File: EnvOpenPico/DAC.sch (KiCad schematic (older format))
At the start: 21 parts, among them U3 PCM5100, U4 PAM8901

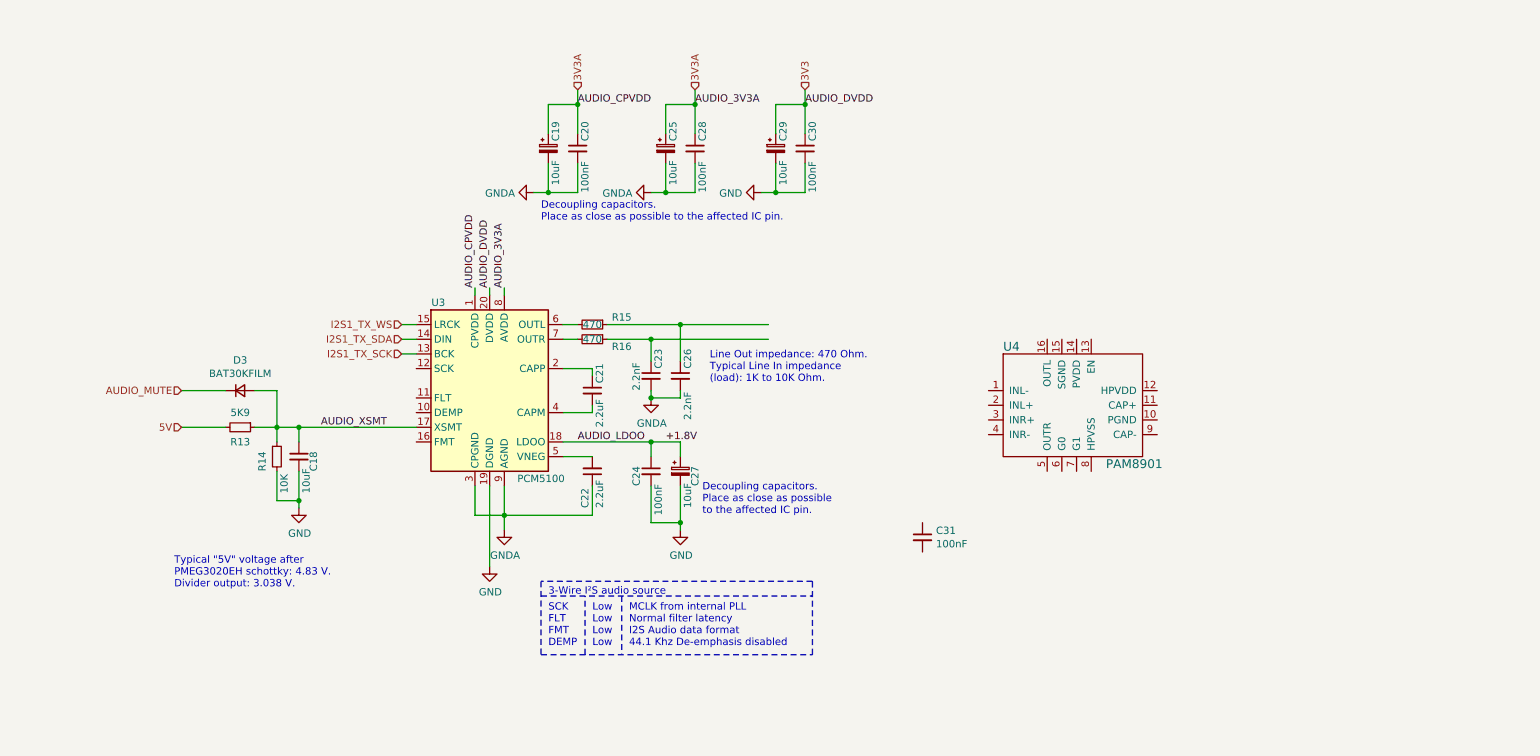
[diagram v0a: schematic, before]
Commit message: Adding audio out, adding pdf schematics
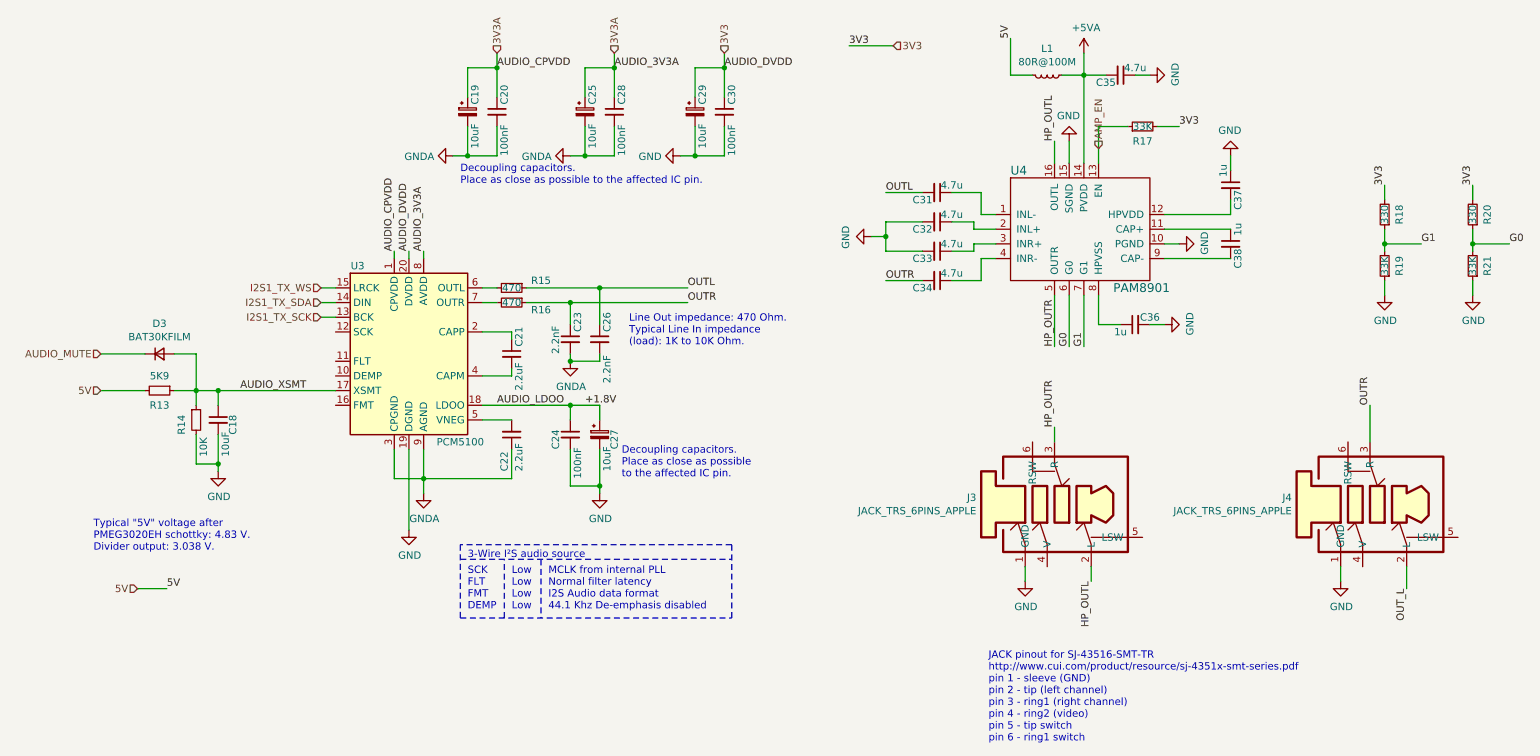
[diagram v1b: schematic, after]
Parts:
- added C32, C33, C34, C35: 4.7u, symbol Device:C_Small
- added C36, C37, C38: 1u, symbol Device:C_Small
- added J3, J4: JACK_TRS_6PINS_APPLE, symbol jack_trs_6pins_apple:JACK_TRS_6PINS_APPLE
- added L1: 80R@100M, symbol Device:L_Small
- added R17, R19, R21: 33K, symbol Device:R_Small
- added R18, R20: 330, symbol Device:R_Small
- C31: value 100nF -> 4.7u
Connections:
- net 3V3: now also R17.2, R18.2, R20.2
- net 5V: now also L1.2
- net GND: now also U4.10 (PGND), U4.15 (SGND), C32.2, C33.2, C35.1, C36.2, C37.1, J3.1 (GND), J4.1 (GND), R19.1, R21.1
- net at U4.1 (INL-): now also C31.1
- net at U4.11 (CAP+): now also C38.1
- net at U4.12 (HPVDD): now also C37.2
- net AMP_EN: now reaches U4.13 (EN)
- net AMP_EN: now also R17.1
- net +5VA: now reaches U4.14 (PVDD)
- net +5VA: now also C35.2, L1.1
- net HP_OUTL: now reaches U4.16 (OUTL)
- net HP_OUTL: now also J3.2 (L)
- net at U4.2 (INL+): now also C32.1
- net at U4.3 (INR+): now also C33.1
- net at U4.4 (INR-): now also C34.1
- net HP_OUTR: now reaches U4.5 (OUTR)
- net HP_OUTR: now also J3.3 (R)
- net G0: now reaches U4.6 (G0)
- net G0: now also R20.1, R21.2
- net G1: now reaches U4.7 (G1)
- net G1: now also R18.1, R19.2
- net at U4.8 (HPVSS): now also C36.1
- net at U4.9 (CAP-): now also C38.2
- net OUTL: now reaches C26.1, R15.1
- net OUTL: now also C31.2
- net OUTR: now reaches C23.1, R16.1
- net OUTR: now also C34.2, J4.3 (R)
- new net OUT_L: J4.2 (L)
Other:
- note added: "JACK pinout for SJ-43516-SMT-TR\nhttp://www.cui.com/product/resource/sj-4351x-smt-series.pdf\npin 1 - sleeve (GND)\npin 2 - tip (left channel)\npin 3 - ring1 (right channel)\npin 4 - ring2 (video)\npin 5 - tip switch\npin 6 - ring1 switch"
- moved on the sheet: C18, C19, C20, C21, C22, C23, C24, C25, C26, C27, C28, C29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

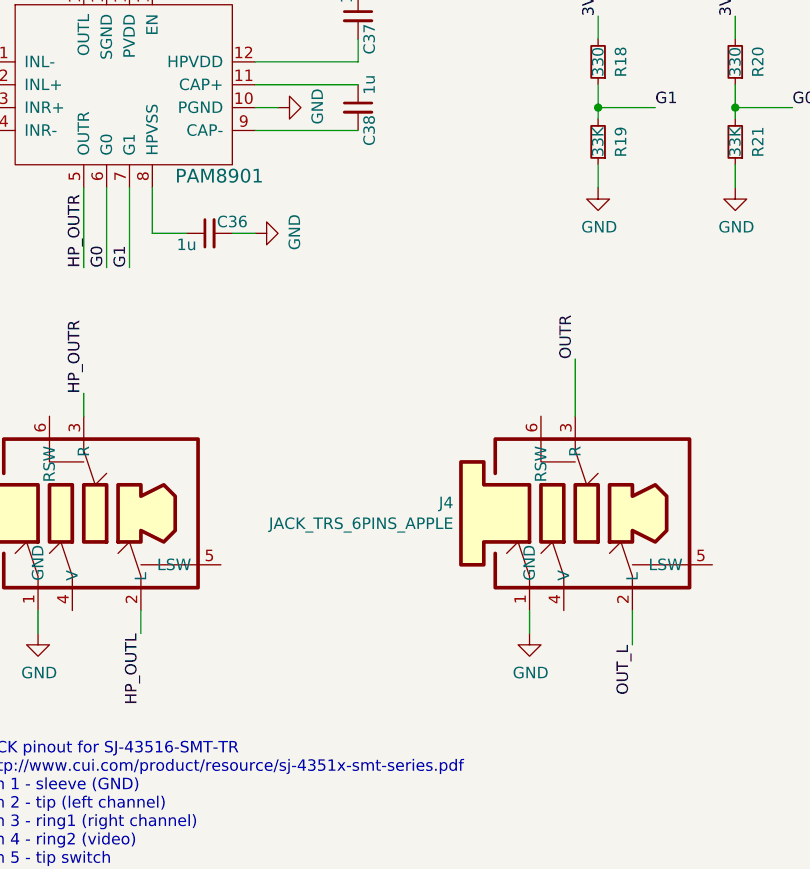
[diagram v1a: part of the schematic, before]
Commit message: Adding parts to pcb
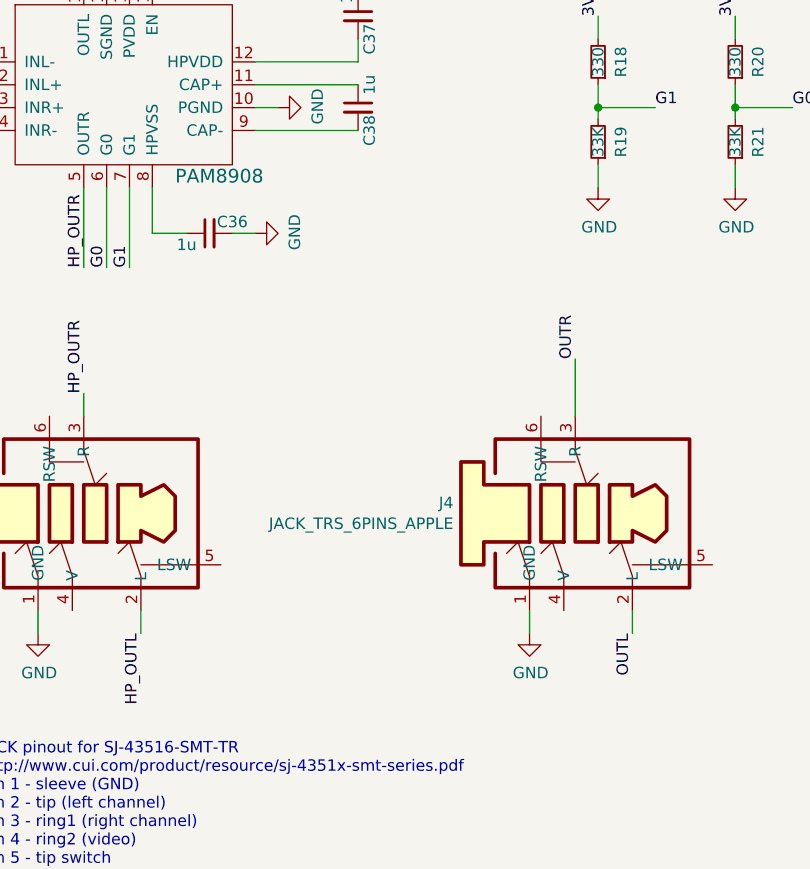
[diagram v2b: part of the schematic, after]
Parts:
- C18, C19, C25, C27, C29: footprint (none) -> Capacitor_SMD:C_1206_3216Metric
- C20, C24, C28, C30, C31, C32, C33, C34, C35, C36, C37, C38: footprint (none) -> Capacitor_SMD:C_0603_1608Metric
- C21, C22, C23, C26, R13, R14, R15, R16, R17, R18, R19, R20, R21: footprint (none) -> Capacitor_SMD:C_0402_1005Metric
- D3: footprint (none) -> Diode_SMD:D_SOD-523
- J3, J4: footprint (none) -> audio-jack:CUI_SJ-43516-SMT
- L1: footprint (none) -> Inductor_SMD:L_0603_1608Metric
- U4: value PAM8901 -> PAM8908; footprint (none) -> Package_DFN_QFN:QFN-16-1EP_3x3mm_P0.5mm_EP1.7x1.7mm_ThermalVias
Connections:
- net OUT_L is gone; now on net OUTL: J4.2 (L)
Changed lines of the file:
@@
 P 7450 1850
 F 0 "U4" H 7250 2050 60  0000 L CNN
-F 1 "PAM8901" H 7950 1250 60  0000 L CNN
-F 2 "" H 7450 2000 60  0001 C CNN
+F 1 "PAM8908" H 7950 1250 60  0000 L CNN
+F 2 "Package_DFN_QFN:QFN-16-1EP_3x3mm_P0.5mm_EP1.7x1.7mm_ThermalVias" H 7450 2000 60  0001 C CNN
 F 3 "" H 7450 2000 60  0001 C CNN
 	1    7450 1850
@@
 F 0 "C21" V 3900 2950 50  0000 L CNN
 F 1 "2.2uF" V 3900 2650 50  0000 L CNN
-F 2 "" H 3850 2900 50  0001 C CNN
-F 3 "~" H 3850 2900 50  0001 C CNN
+F 2 "Capacitor_SMD:C_0402_1005Metric" H 3850 2900 50  0001 C CNN
+F 3 "CL10A225KO8NNNC " H 3850 2900 50  0001 C CNN
 	1    3850 2900
 	1    0    0    -1
@@
 F 0 "C22" V 3900 3700 50  0000 R CNN
 F 1 "2.2uF" V 3800 3700 50  0000 R CNN
-F 2 "" H 3850 3450 50  0001 C CNN
-F 3 "~" H 3850 3450 50  0001 C CNN
+F 2 "Capacitor_SMD:C_0402_1005Metric" H 3850 3450 50  0001 C CNN
+F 3 "CL10A225KO8NNNC " H 3850 3450 50  0001 C CNN
 	1    3850 3450
 	-1   0    0    1
@@
 F 0 "R15" V 3800 2650 50  0000 C CNN
 F 1 "470" V 3850 2450 50  0000 C CNN
-F 2 "" H 3850 2450 50  0001 C CNN
+F 2 "Capacitor_SMD:C_0402_1005Metric" H 3850 2450 50  0001 C CNN
 F 3 "~" H 3850 2450 50  0001 C CNN
 	1    3850 2450
@@
 F 0 "R16" V 3900 2750 50  0000 C CNN
 F 1 "470" V 3850 2550 50  0000 C CNN
-F 2 "" H 3850 2550 50  0001 C CNN
+F 2 "Capacitor_SMD:C_0402_1005Metric" H 3850 2550 50  0001 C CNN
 F 3 "~" H 3850 2550 50  0001 C CNN
 	1    3850 2550
@@
 F 0 "C26" V 4500 2850 50  0000 L CNN
 F 1 "2.2nF" V 4500 2500 50  0000 L CNN
-F 2 "" H 4450 2800 50  0001 C CNN
+F 2 "Capacitor_SMD:C_0402_1005Metric" H 4450 2800 50  0001 C CNN
 F 3 "885012206061" H 4450 2800 50  0001 C CNN
 	1    4450 2800
@@
 F 0 "C23" V 4300 2850 50  0000 L CNN
 F 1 "2.2nF" V 4150 2700 50  0000 L CNN
-F 2 "" H 4250 2800 50  0001 C CNN
+F 2 "Capacitor_SMD:C_0402_1005Metric" H 4250 2800 50  0001 C CNN
 F 3 "885012206061" H 4250 2800 50  0001 C CNN
 	1    4250 2800
@@
 F 0 "C20" V 3800 1300 50  0000 L CNN
 F 1 "100nF" V 3800 950 50  0000 L CNN
-F 2 "" H 3750 1250 50  0001 C CNN
+F 2 "Capacitor_SMD:C_0603_1608Metric" H 3750 1250 50  0001 C CNN
 F 3 "885012206071" H 3750 1250 50  0001 C CNN
 	1    3750 1250
@@
 F 0 "C19" V 3600 1300 50  0000 L CNN
 F 1 "10uF" V 3600 1000 50  0000 L CNN
-F 2 "" H 3550 1250 50  0001 C CNN
+F 2 "Capacitor_SMD:C_1206_3216Metric" H 3550 1250 50  0001 C CNN
 F 3 "TAJA106K016RNJ" H 3550 1250 50  0001 C CNN
 	1    3550 1250
@@
 F 0 "C25" V 4400 1300 50  0000 L CNN
 F 1 "10uF" V 4400 1000 50  0000 L CNN
-F 2 "" H 4350 1250 50  0001 C CNN
+F 2 "Capacitor_SMD:C_1206_3216Metric" H 4350 1250 50  0001 C CNN
 F 3 "TAJA106K016RNJ" H 4350 1250 50  0001 C CNN
 	1    4350 1250
@@
 F 0 "C28" V 4600 1300 50  0000 L CNN
 F 1 "100nF" V 4600 950 50  0000 L CNN
-F 2 "" H 4550 1250 50  0001 C CNN
+F 2 "Capacitor_SMD:C_0603_1608Metric" H 4550 1250 50  0001 C CNN
 F 3 "885012206071" H 4550 1250 50  0001 C CNN
 	1    4550 1250
@@
 F 0 "C29" V 5150 1300 50  0000 L CNN
 F 1 "10uF" V 5150 1000 50  0000 L CNN
-F 2 "" H 5100 1250 50  0001 C CNN
+F 2 "Capacitor_SMD:C_1206_3216Metric" H 5100 1250 50  0001 C CNN
 F 3 "TAJA106K016RNJ" H 5100 1250 50  0001 C CNN
 	1    5100 1250
@@
 F 0 "C30" V 5350 1300 50  0000 L CNN
 F 1 "100nF" V 5350 950 50  0000 L CNN
-F 2 "" H 5300 1250 50  0001 C CNN
+F 2 "Capacitor_SMD:C_0603_1608Metric" H 5300 1250 50  0001 C CNN
 F 3 "885012206071" H 5300 1250 50  0001 C CNN
 	1    5300 1250
@@
 F 0 "C24" V 4150 3350 50  0000 L CNN
 F 1 "100nF" V 4300 3150 50  0000 L CNN
-F 2 "" H 4250 3450 50  0001 C CNN
+F 2 "Capacitor_SMD:C_0603_1608Metric" H 4250 3450 50  0001 C CNN
 F 3 "885012206071" H 4250 3450 50  0001 C CNN
 	1    4250 3450
@@
 F 0 "C27" V 4550 3350 50  0000 L CNN
 F 1 "10uF" V 4500 3200 50  0000 L CNN
-F 2 "" H 4450 3450 50  0001 C CNN
+F 2 "Capacitor_SMD:C_1206_3216Metric" H 4450 3450 50  0001 C CNN
 F 3 "TAJA106K016RNJ" H 4450 3450 50  0001 C CNN
 	1    4450 3450
@@
 F 0 "D3" H 1450 3107 50  0000 C CNN
 F 1 "BAT30KFILM" H 1450 3016 50  0000 C CNN
-F 2 "" V 1450 2900 50  0001 C CNN
+F 2 "Diode_SMD:D_SOD-523" V 1450 2900 50  0001 C CNN
 F 3 "~" V 1450 2900 50  0001 C CNN
 	1    1450 2900
@@
 F 0 "C18" V 1950 3250 50  0000 L CNN
 F 1 "10uF" V 1900 3100 50  0000 L CNN
-F 2 "" H 1850 3350 50  0001 C CNN
+F 2 "Capacitor_SMD:C_1206_3216Metric" H 1850 3350 50  0001 C CNN
 F 3 "EMK316B7106KL-TD" H 1850 3350 50  0001 C CNN
 	1    1850 3350
@@
 F 0 "R14" V 1600 3250 50  0000 L CNN
 F 1 "10K" V 1750 3100 50  0000 L CNN
-F 2 "" H 1700 3350 50  0001 C CNN
+F 2 "Capacitor_SMD:C_0402_1005Metric" H 1700 3350 50  0001 C CNN
 F 3 "~" H 1700 3350 50  0001 C CNN
 	1    1700 3350
@@
 F 0 "R13" V 1550 3150 50  0000 C CNN
 F 1 "5K9" V 1350 3150 50  0000 C CNN
-F 2 "" H 1450 3150 50  0001 C CNN
+F 2 "Capacitor_SMD:C_0402_1005Metric" H 1450 3150 50  0001 C CNN
 F 3 "~" H 1450 3150 50  0001 C CNN
 	1    1450 3150
@@
 F 0 "C31" V 6800 1700 50  0000 C CNN
 F 1 "4.7u" V 6700 1900 50  0000 C CNN
-F 2 "" H 6750 1800 50  0001 C CNN
-F 3 "~" H 6750 1800 50  0001 C CNN
+F 2 "Capacitor_SMD:C_0603_1608Metric" H 6750 1800 50  0001 C CNN
+F 3 "CL10A475KP8NNNC " H 6750 1800 50  0001 C CNN
 	1    6750 1800
 	0    1    1    0
@@
 F 0 "C32" V 6800 1900 50  0000 C CNN
 F 1 "4.7u" V 6700 2100 50  0000 C CNN
-F 2 "" H 6750 2000 50  0001 C CNN
-F 3 "~" H 6750 2000 50  0001 C CNN
+F 2 "Capacitor_SMD:C_0603_1608Metric" H 6750 2000 50  0001 C CNN
+F 3 "CL10A475KP8NNNC " H 6750 2000 50  0001 C CNN
 	1    6750 2000
 	0    1    1    0
@@
 F 0 "C33" V 6800 2100 50  0000 C CNN
 F 1 "4.7u" V 6700 2300 50  0000 C CNN
-F 2 "" H 6750 2200 50  0001 C CNN
-F 3 "~" H 6750 2200 50  0001 C CNN
+F 2 "Capacitor_SMD:C_0603_1608Metric" H 6750 2200 50  0001 C CNN
+F 3 "CL10A475KP8NNNC " H 6750 2200 50  0001 C CNN
 	1    6750 2200
 	0    1    1    0
@@
 F 0 "C34" V 6800 2300 50  0000 C CNN
 F 1 "4.7u" V 6700 2500 50  0000 C CNN
-F 2 "" H 6750 2400 50  0001 C CNN
-F 3 "~" H 6750 2400 50  0001 C CNN
+F 2 "Capacitor_SMD:C_0603_1608Metric" H 6750 2400 50  0001 C CNN
+F 3 "CL10A475KP8NNNC " H 6750 2400 50  0001 C CNN
 	1    6750 2400
 	0    1    1    0
@@
 F 0 "C36" V 8150 2600 50  0000 C CNN
 F 1 "1u" V 8050 2800 50  0000 C CNN
-F 2 "" H 8100 2700 50  0001 C CNN
-F 3 "~" H 8100 2700 50  0001 C CNN
+F 2 "Capacitor_SMD:C_0603_1608Metric" H 8100 2700 50  0001 C CNN
+F 3 "CL10A105KQ8NNNC " H 8100 2700 50  0001 C CNN
 	1    8100 2700
 	0    -1   -1   0
@@
 F 0 "C38" V 8800 2050 50  0000 C CNN
 F 1 "1u" V 8800 2250 50  0000 C CNN
-F 2 "" H 8750 2150 50  0001 C CNN
-F 3 "~" H 8750 2150 50  0001 C CNN
+F 2 "Capacitor_SMD:C_0603_1608Metric" H 8750 2150 50  0001 C CNN
+F 3 "CL10A105KQ8NNNC " H 8750 2150 50  0001 C CNN
 	1    8750 2150
 	1    0    0    -1
@@
 F 0 "C37" V 8800 1650 50  0000 C CNN
 F 1 "1u" V 8700 1850 50  0000 C CNN
-F 2 "" H 8750 1750 50  0001 C CNN
-F 3 "~" H 8750 1750 50  0001 C CNN
+F 2 "Capacitor_SMD:C_0603_1608Metric" H 8750 1750 50  0001 C CNN
+F 3 "CL10A105KQ8NNNC " H 8750 1750 50  0001 C CNN
 	1    8750 1750
 	1    0    0    -1
@@
 F 0 "C35" V 8050 900 50  0000 C CNN
 F 1 "4.7u" V 7950 1100 50  0000 C CNN
-F 2 "" H 8000 1000 50  0001 C CNN
-F 3 "~" H 8000 1000 50  0001 C CNN
+F 2 "Capacitor_SMD:C_0603_1608Metric" H 8000 1000 50  0001 C CNN
+F 3 "CL10A475KP8NNNC " H 8000 1000 50  0001 C CNN
 	1    8000 1000
 	0    1    1    0
@@
 F 0 "L1" V 7319 1000 50  0000 C CNN
 F 1 "80R@100M" V 7410 1000 50  0000 C CNN
-F 2 "" H 7500 1000 50  0001 C CNN
+F 2 "Inductor_SMD:L_0603_1608Metric" H 7500 1000 50  0001 C CNN
 F 3 "~" H 7500 1000 50  0001 C CNN
 	1    7500 1000
@@
 F 0 "R19" V 9700 2300 50  0000 C CNN
 F 1 "33K" V 9800 2300 50  0000 C CNN
-F 2 "" H 9800 2300 50  0001 C CNN
+F 2 "Capacitor_SMD:C_0402_1005Metric" H 9800 2300 50  0001 C CNN
 F 3 "~" H 9800 2300 50  0001 C CNN
 	1    9800 2300
@@
 F 0 "R18" V 9700 1950 50  0000 C CNN
 F 1 "330" V 9800 1950 50  0000 C CNN
-F 2 "" H 9800 1950 50  0001 C CNN
+F 2 "Capacitor_SMD:C_0402_1005Metric" H 9800 1950 50  0001 C CNN
 F 3 "~" H 9800 1950 50  0001 C CNN
 	1    9800 1950
@@
 F 0 "R20" V 10300 1950 50  0000 C CNN
 F 1 "330" V 10400 1950 50  0000 C CNN
-F 2 "" H 10400 1950 50  0001 C CNN
+F 2 "Capacitor_SMD:C_0402_1005Metric" H 10400 1950 50  0001 C CNN
 F 3 "~" H 10400 1950 50  0001 C CNN
 	1    10400 1950
@@
 F 0 "R21" V 10300 2300 50  0000 C CNN
 F 1 "33K" V 10400 2300 50  0000 C CNN
-F 2 "" H 10400 2300 50  0001 C CNN
+F 2 "Capacitor_SMD:C_0402_1005Metric" H 10400 2300 50  0001 C CNN
 F 3 "~" H 10400 2300 50  0001 C CNN
 	1    10400 2300
@@
 F 0 "R17" V 8050 1350 50  0000 C CNN
 F 1 "33K" V 8150 1350 50  0000 C CNN
-F 2 "" H 8150 1350 50  0001 C CNN
+F 2 "Capacitor_SMD:C_0402_1005Metric" H 8150 1350 50  0001 C CNN
 F 3 "~" H 8150 1350 50  0001 C CNN
 	1    8150 1350
@@
 F 0 "J4" H 9167 4021 50  0000 R CNN
 F 1 "JACK_TRS_6PINS_APPLE" H 9167 3930 50  0000 R CNN
-F 2 "" H 10050 4200 60  0000 C CNN
+F 2 "audio-jack:CUI_SJ-43516-SMT" H 10050 4200 60  0001 C CNN
 F 3 "" H 10050 4200 60  0000 C CNN
 	1    9950 3950
@@
 F 0 "J3" H 7017 4021 50  0000 R CNN
 F 1 "JACK_TRS_6PINS_APPLE" H 7017 3930 50  0000 R CNN
-F 2 "" H 7900 4200 60  0000 C CNN
+F 2 "audio-jack:CUI_SJ-43516-SMT" H 7900 4200 60  0001 C CNN
 F 3 "" H 7900 4200 60  0000 C CNN
 	1    7800 3950
@@
 Text Label 9700 3250 1    50   ~ 0
 OUTR
-Text Label 9950 4500 3    50   ~ 0
-OUT_L
-Wire Wire Line
-	9950 4500 9950 4350
+Text Label 9950 4450 3    50   ~ 0
+OUTL
 $Comp
 L power:GND #PWR049
@@
 Text Notes 7100 5550 0    50   ~ 0
 JACK pinout for SJ-43516-SMT-TR\nhttp://www.cui.com/product/resource/sj-4351x-smt-series.pdf\npin 1 - sleeve (GND)\npin 2 - tip (left channel)\npin 3 - ring1 (right channel)\npin 4 - ring2 (video)\npin 5 - tip switch\npin 6 - ring1 switch
+Wire Wire Line
+	9950 4350 9950 4450
 $EndSCHEMATC
